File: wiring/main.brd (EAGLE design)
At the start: 100 x 80 mm, 39 parts, among them IC1 attiny 2313A, J1 J7MM, J2 J10MM, J3 J5MM, J4 J10MM, J5 J7MM, J6 J5MM, J7 J5MM, Q1 12MHz, T1 BD433, X1 USB-B

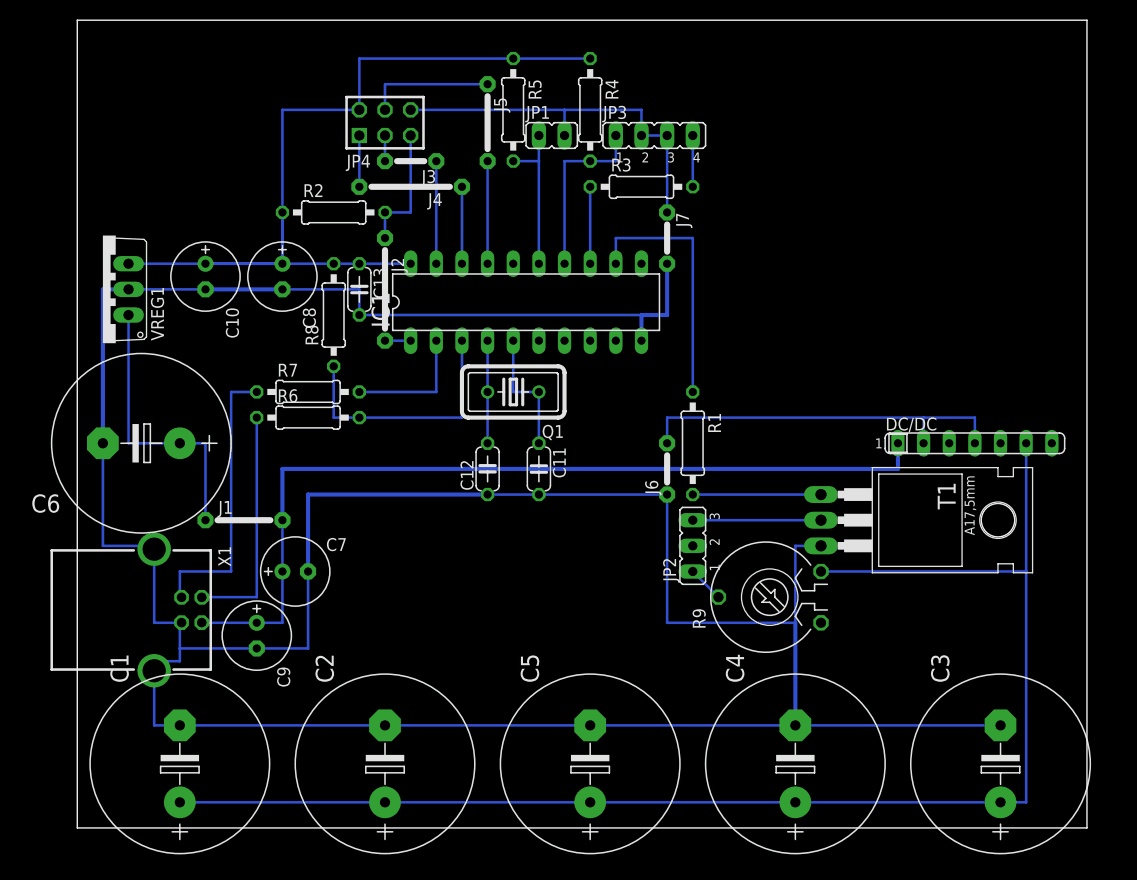
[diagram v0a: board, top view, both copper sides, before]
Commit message: add wiring/board.png
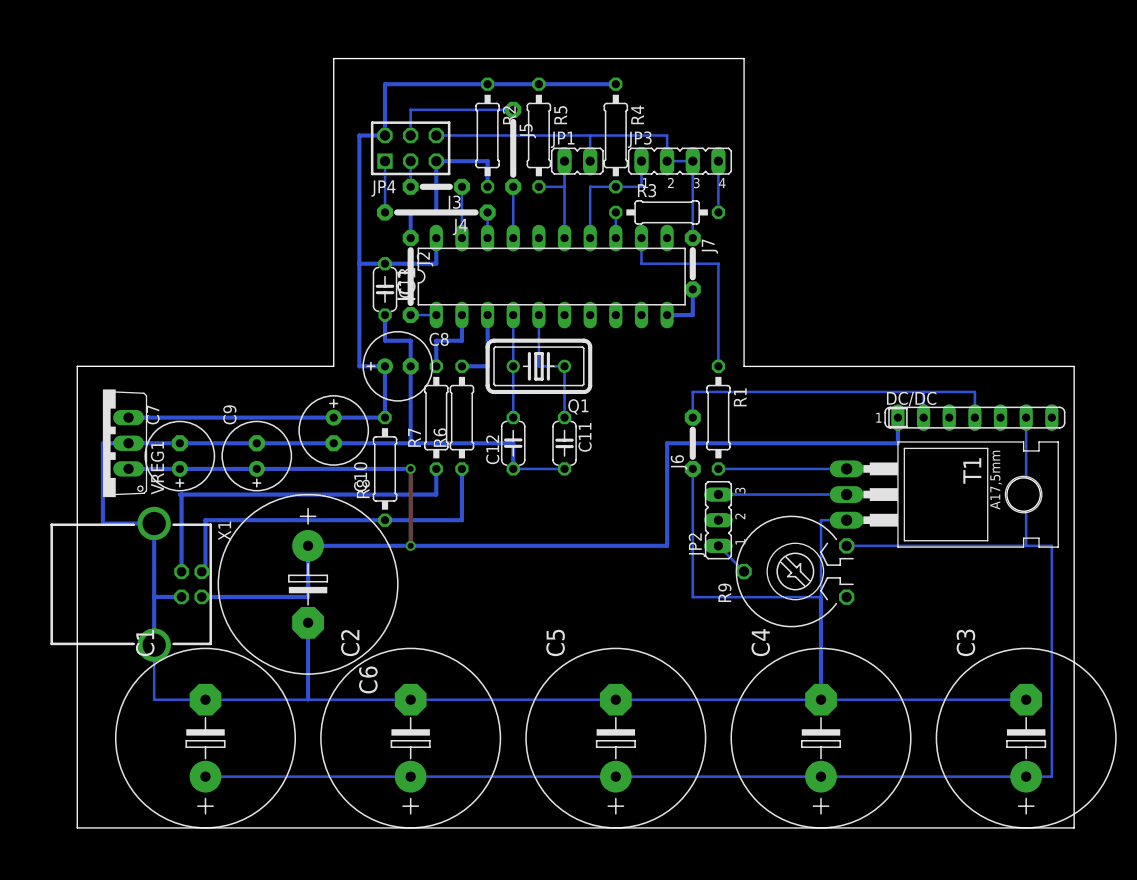
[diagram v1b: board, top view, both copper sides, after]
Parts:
- removed J1: J7MM, jumper:07
- J2: value J10MM -> J7MM; device jumper:10 -> jumper:07
- moved C6 21.6 mm to (22.9, 24.1), turned to 270 degrees
- moved C10 19.8 mm to (25.4, 39.4)
- moved C9 17.8 mm to (17.8, 36.8), turned to 90 degrees
- moved R2 17.0 mm to (40.6, 68.6), turned to 270 degrees
- moved C7 16.2 mm to (10.2, 36.8), turned to 90 degrees
- moved R8 16.1 mm to (30.5, 35.6)
- moved R6 15.2 mm to (38.1, 40.6), turned to 90 degrees
- moved VREG1 15.2 mm to (2.54, 38.1)
- moved C8 14.5 mm to (31.8, 45.7), turned to 0 degrees
- moved R7 13.0 mm to (35.6, 40.6), turned to 90 degrees
- moved R4 3.59 mm to (53.3, 68.6)
- moved C3 3.59 mm to (94.0, 8.89)
- moved C5 3.59 mm to (53.3, 8.89)
- moved J3 3.59 mm to (35.6, 63.5)
- moved R5 3.59 mm to (45.7, 68.6)
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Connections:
- removed net N$6: C6.+, J1.1, VREG1.1
- net 5V: now also C6.+, VREG1.1; no longer J1.2
- net N$16: now also R8.1
- net N$19: no longer R8.1
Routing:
- net GND: track 313.9 -> 241.5 mm
- net 5V: track 86.7 -> 122.3 mm, vias 0 -> 2
- net N$6: track 27.9 -> 0.00 mm
- net N$19: track 25.4 -> 7.62 mm
- net N$16: track 23.2 -> 36.0 mm
- net N$17: track 28.1 -> 35.6 mm
- net RST: track 12.7 -> 17.8 mm
- net SCK: track 10.2 -> 5.08 mm
- net MOSI: track 10.2 -> 5.08 mm
- net N$18: track 12.7 -> 7.62 mm
- net VCC: track 91.4 -> 96.5 mm
- net N$14: track 7.62 -> 2.54 mm
- net N$1: track 25.4 -> 20.3 mm
- net MISO: track 7.62 -> 2.54 mm
- net N$15: track 17.8 -> 12.7 mm
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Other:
- board size 100 x 80 mm -> 98.7 x 76.2 mm

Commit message: ändern auf mosfet
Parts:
- removed J6: J5MM, jumper:05
- removed R9: 1k, pot:PT-10
- removed T1: BD433, transistor:TO220
- added C14: 220µ, resistor:E2,5-7
- added D1: 1N4148DO35-7, diode:DO35-7
- added IRF3708: IRF3704L-V, transistor-power:TO262-V
- added R10: 10k, rcl:0207/10
- R1: value 1k -> 100
- moved DC/DC 49.1 mm to (43.2, 22.9)
- moved C3 34.1 mm to (63.5, 24.1), turned to 270 degrees
- moved JP2 10.2 mm to (63.5, 40.6)
- moved R1 10.2 mm to (63.5, 50.8)
- moved C8 2.54 mm to (29.2, 45.7)
- turned C1 to 270 degrees
- turned C2 to 270 degrees
- turned C4 to 270 degrees
- turned C5 to 270 degrees
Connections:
- removed net N$21: DC/DC.2, DC/DC.4, J6.2
- removed net N$5: JP2.1, R9.S
- net 5V: now also C14.+
- net GND: now also C14.-, DC/DC.2, DC/DC.4, IRF3708.3, R10.1; no longer J6.1, T1.3
- net N$2: now also IRF3708.1, R10.2; no longer T1.1
- net N$3: now also D1.A, IRF3708.2; no longer T1.2
- net N$4: now also D1.C, JP2.1; no longer R9.E
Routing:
- net GND: track 241.5 -> 340.5 mm
- net 5V: track 122.3 -> 81.6 mm
- net N$21: track 35.6 -> 0.00 mm
- net N$4: track 139.7 -> 106.7 mm
- net N$1: track 20.3 -> 10.2 mm
- net N$5: track 3.59 -> 0.00 mm
- net N$3: track 12.7 -> 10.2 mm
- net N$22: track 38.1 -> 40.6 mm
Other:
- board size 98.7 x 76.2 mm -> 75.9 x 73.7 mm

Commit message: zwischenspeichern schaltplan schöner zeichnen
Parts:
- R2: value 100k -> 10k
- turned J2 to 90 degrees
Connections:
- net N$1 renamed PB0
- net N$16 renamed D-
- net N$17 renamed D+
- net N$4 renamed +15V
- removed net N$7: IC1.1, J2.2
- removed net RST: J2.1, JP4.5, R2.2
- new net N$1: IC1.1, J2.1
- new net RST1: J2.2, JP4.5, R2.2
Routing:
- net RST1: track 0.00 -> 17.8 mm
- net RST: track 17.8 -> 0.00 mm
- net VCC: track 96.5 -> 81.3 mm
- net GND: track 340.5 -> 330.4 mm
- net N$7: track 2.54 -> 0.00 mm
- net N$1: track 0.00 -> 2.54 mm

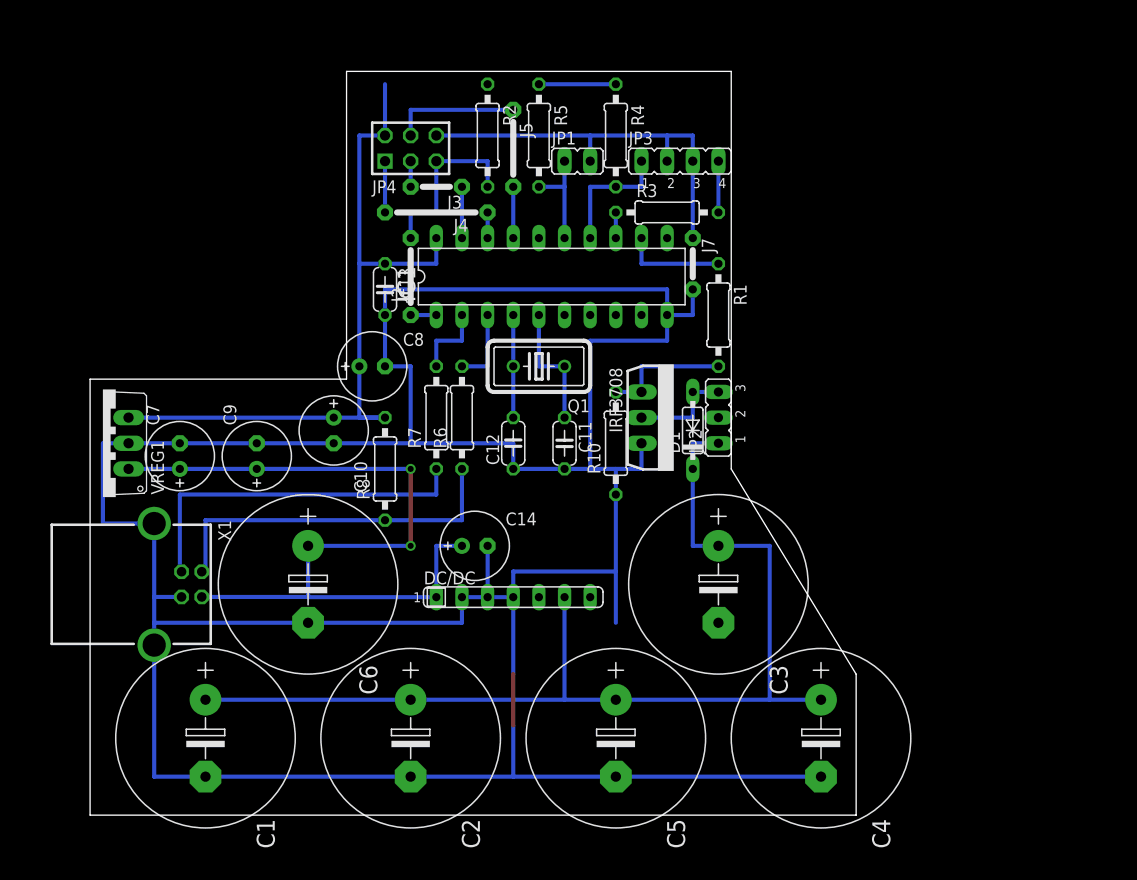
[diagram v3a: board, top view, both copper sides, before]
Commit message: schaltplan überarbeitet
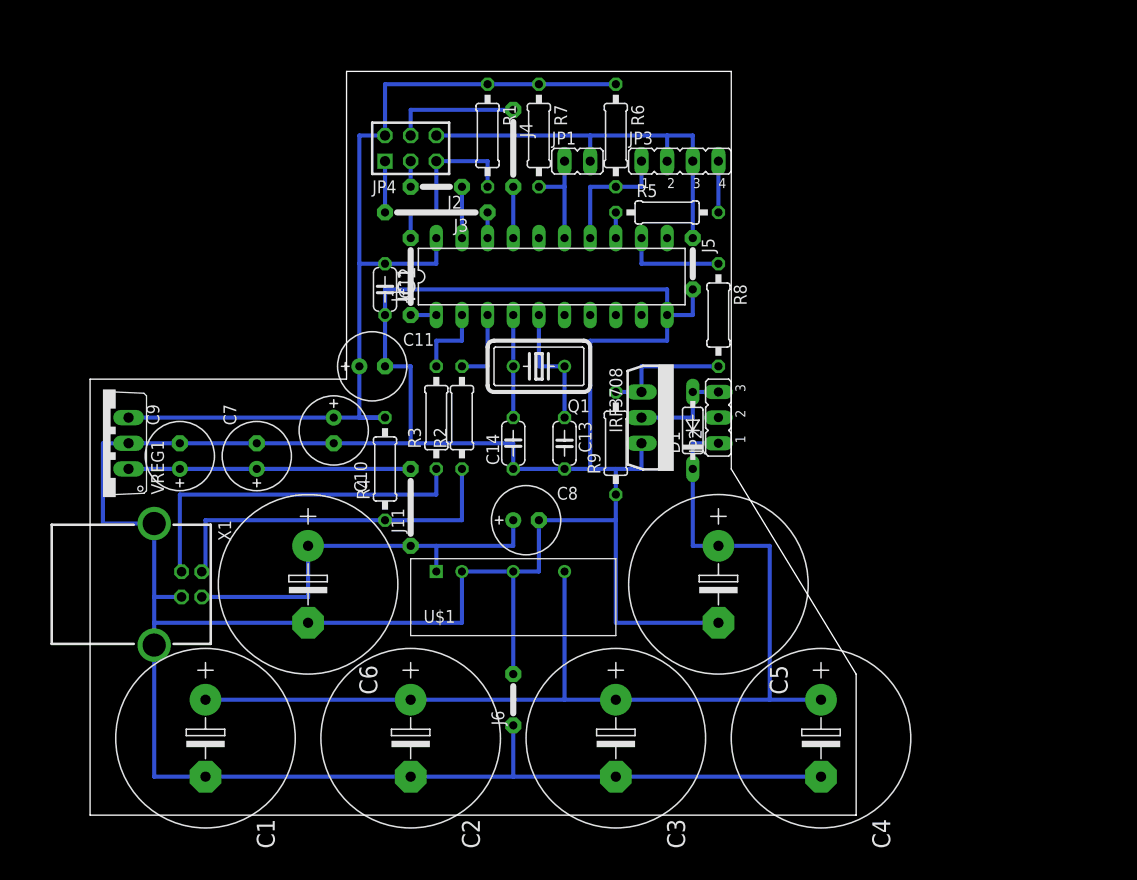
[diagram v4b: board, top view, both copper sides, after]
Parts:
- removed DC/DC: doof, resistor-sil:SIL7
- removed J7: J5MM, jumper:05
- added J1, J11: J7MM, jumper:07
- added J6: J5MM, jumper:05
- added U$1: SIM2-0515S, eigene:SIL7
- C11: value 22p -> 68µ; device rcl:C050-024X044 -> resistor:E2,5-7
- C12: value 22p -> 330p
- C13: value 330p -> 22p
- C14: value 220µ -> 22p; device resistor:E2,5-7 -> rcl:C050-024X044
- C7, C8: value 68µ -> 220µ
- C9: value 220µ -> 68µ
- J2, J5: value J7MM -> J5MM; device jumper:07 -> jumper:05
- J3: value J5MM -> J10MM; device jumper:05 -> jumper:10
- J4: value J10MM -> J7MM; device jumper:10 -> jumper:07
- R1: value 100 -> 10k
- R2, R5: value 10k -> 68
- R4: value 10k -> 1,5k
- R6, R7: value 68 -> 10k
- R8: value 1,5k -> 100
- moved R4 40.2 mm to (30.5, 35.6), turned to 90 degrees
- moved R8 36.4 mm to (63.5, 50.8), turned to 270 degrees
- moved R6 31.8 mm to (53.3, 68.6), turned to 270 degrees
- moved R3 30.6 mm to (35.6, 40.6), turned to 90 degrees
- moved R7 29.7 mm to (45.7, 68.6), turned to 270 degrees
- moved R1 29.0 mm to (40.6, 68.6)
- moved R2 28.1 mm to (38.1, 40.6), turned to 90 degrees
- moved C13 23.4 mm to (48.3, 38.1)
- moved C8 21.6 mm to (44.5, 30.5)
- moved J5 21.1 mm to (61.0, 55.9)
- moved C11 20.5 mm to (29.2, 45.7), turned to 0 degrees
- moved C12 19.8 mm to (30.5, 53.3), turned to 270 degrees
- moved C3 18.3 mm to (53.3, 8.89)
- moved C5 18.3 mm to (63.5, 24.1)
- moved R5 14.8 mm to (58.4, 61.0), turned to 0 degrees
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- renumbered R10 to R9
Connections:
- removed net 5V: C14.+, C6.+, C7.+, C9.+, DC/DC.1, VREG1.1, X1.1
- removed net N$1: IC1.1, J2.1
- removed net N$10: J4.2, JP4.1
- removed net N$20: J5.1, JP4.4
- removed net N$22: J7.1, JP1.2, JP3.2, JP3.3, JP4.6
- removed net N$9: J3.2, JP4.3
- removed net RST1: J2.2, JP4.5, R2.2
- new net +5V: C6.+, C7.+, C8.+, C9.+, J11.1, J11.2, U$1.PIN1, VREG1.1, X1.1
- new net RST: IC1.1, J1.1, J1.2, JP4.5, R1.2
- net +15V: now also U$1.PIN6; no longer DC/DC.6
- net D+: now also R3.1; no longer R7.1
- net D-: now also R2.1, R4.1; no longer R6.1, R8.1
- net GND: now also C11.-, C12.2, C14.1, J5.1, J5.2, J6.1, J6.2, JP1.2, JP3.2, JP3.3, JP4.6, U$1.PIN2, U$1.PIN4; no longer C11.2, C12.1, C14.-, DC/DC.2, DC/DC.4, J7.2
- net MISO: now also J3.1, J3.2, JP4.1; no longer J4.1
- net MOSI: now also J4.1, J4.2, JP4.4; no longer J5.2
- net N$11: now also C13.1; no longer C11.1
- net N$12: now also C14.2; no longer C12.2
- net N$13: now also R7.2; no longer R5.2
- net N$14: now also R5.1; no longer R3.1
- net N$15: now also R6.2; no longer R4.2
- net N$18: now also R3.2; no longer R7.2
- net N$19: now also R2.2; no longer R6.2
- net N$2: now also R8.2; no longer R1.2
- net N$8: now also R5.2; no longer R3.2
- net PB0: now also R8.1; no longer R1.1
- net SCK: now also J2.1, J2.2, JP4.3; no longer J3.1
- net VCC: now also C11.+, C12.1, R1.1, R4.2, R6.1, R7.1; no longer C13.1, C8.+, R2.1, R4.1, R5.1, R8.2
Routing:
- net 5V: track 81.6 -> 0.00 mm, vias 2 -> 0
- net +5V: track 0.00 -> 69.0 mm
- net GND: track 330.4 -> 378.6 mm
- net N$22: track 40.6 -> 0.00 mm
- net RST: track 0.00 -> 20.3 mm
- net RST1: track 17.8 -> 0.00 mm
- net VCC: track 81.3 -> 96.5 mm
- net N$20: track 12.7 -> 0.00 mm
- net MOSI: track 5.08 -> 17.8 mm
- net N$10: track 5.08 -> 0.00 mm
- net MISO: track 2.54 -> 7.62 mm
- net SCK: track 5.08 -> 7.62 mm
- net N$9: track 2.54 -> 0.00 mm
- net +15V: track 106.7 -> 109.2 mm
- net N$1: track 2.54 -> 0.00 mm

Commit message: kleine Aenderungen
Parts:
- moved C8 4.02 mm to (40.6, 31.8), turned to 90 degrees
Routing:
- net GND: track 378.6 -> 386.3 mm
- net +5V: track 69.0 -> 66.4 mm
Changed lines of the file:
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@@
 <element name="IRF3708" library="transistor-power" package="TO262-V" value="IRF3704L-V" x="55.88" y="40.64" rot="R270"/>
 <element name="R9" library="rcl" package="0207/10" value="10k" x="53.34" y="38.1" rot="R90"/>
-<element name="C8" library="resistor" package="E2,5-7" value="220µ" x="44.45" y="30.48"/>
+<element name="C8" library="resistor" package="E2,5-7" value="220µ" x="40.64" y="31.75" rot="R90"/>
 <element name="U$1" library="eigene" package="SIL7" value="SIM2-0515S" x="35.56" y="25.4"/>
 <element name="J11" library="jumper" package="07" value="J7MM" x="33.02" y="31.75" rot="R90"/>
@@
 <wire x1="33.02" y1="27.94" x2="35.56" y2="27.94" width="0.4064" layer="16"/>
 <wire x1="35.56" y1="27.94" x2="35.56" y2="25.4" width="0.4064" layer="16"/>
-<wire x1="35.56" y1="27.94" x2="43.18" y2="27.94" width="0.4064" layer="16"/>
-<wire x1="43.18" y1="27.94" x2="43.18" y2="30.48" width="0.4064" layer="16"/>
+<wire x1="35.56" y1="27.94" x2="40.64" y2="27.94" width="0.4064" layer="16"/>
+<wire x1="40.64" y1="27.94" x2="40.64" y2="30.48" width="0.4064" layer="16"/>
 <wire x1="17.78" y1="35.56" x2="33.02" y2="35.56" width="0.4064" layer="16"/>
 <wire x1="5.08" y1="35.56" x2="10.16" y2="35.56" width="0" layer="19" extent="1-1"/>
@@
 <wire x1="63.5" y1="20.32" x2="53.34" y2="20.32" width="0.4064" layer="16"/>
 <wire x1="53.34" y1="20.32" x2="53.34" y2="30.48" width="0.4064" layer="16"/>
-<wire x1="53.34" y1="30.48" x2="53.34" y2="33.02" width="0.4064" layer="16"/>
-<wire x1="45.72" y1="30.48" x2="53.34" y2="30.48" width="0.4064" layer="16"/>
+<wire x1="40.64" y1="33.02" x2="53.34" y2="33.02" width="0.4064" layer="16"/>
+<wire x1="53.34" y1="33.02" x2="53.34" y2="30.48" width="0.4064" layer="16"/>
 <wire x1="22.86" y1="20.32" x2="38.1" y2="20.32" width="0.4064" layer="16"/>
 <wire x1="38.1" y1="20.32" x2="38.1" y2="25.4" width="0.4064" layer="16"/>
 <wire x1="38.1" y1="25.4" x2="43.18" y2="25.4" width="0.4064" layer="16"/>
-<wire x1="43.18" y1="25.4" x2="45.72" y2="25.4" width="0.4064" layer="16"/>
-<wire x1="45.72" y1="25.4" x2="45.72" y2="30.48" width="0.4064" layer="16"/>
 <contactref element="J5" pad="1"/>
 <contactref element="J5" pad="2"/>
@@
 <wire x1="43.18" y1="5.08" x2="33.02" y2="5.08" width="0.4064" layer="16"/>
 <wire x1="53.34" y1="5.08" x2="43.18" y2="5.08" width="0.4064" layer="16"/>
-<wire x1="43.18" y1="15.24" x2="43.18" y2="25.4" width="0.4064" layer="16"/>
+<wire x1="43.18" y1="15.24" x2="43.18" y2="33.02" width="0.4064" layer="16"/>
+<wire x1="43.18" y1="33.02" x2="40.64" y2="33.02" width="0.4064" layer="16"/>
 <wire x1="60.96" y1="53.34" x2="60.96" y2="58.42" width="0" layer="19" extent="1-1"/>
 <wire x1="10.16" y1="38.1" x2="5.08" y2="38.1" width="0" layer="19" extent="1-1"/>
@@
 </signal>
 </signals>
-<errors>
-</errors>
 </board>
 </drawing>
